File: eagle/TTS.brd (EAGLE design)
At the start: 35.2 x 26.7 mm, 14 parts, among them IC1 LM386N-1

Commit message: updates after build #1
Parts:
- C2, C3: device resistor:C025-025X050 -> rcl:C050-024X044
- R3: value 10k -> 10R
- moved JP1 21.6 mm to (44.5, 33.0), turned to 0 degrees
- moved C6 12.7 mm to (34.3, 44.5)
- moved C2 6.84 mm to (29.2, 41.9), turned to 90 degrees
- moved C3 5.08 mm to (35.6, 39.4), turned to 180 degrees
- moved C1 4.02 mm to (55.9, 33.0), turned to 180 degrees
- moved R2 4.02 mm to (33.0, 35.6), turned to 0 degrees
- moved R1 4.02 mm to (33.0, 33.0), turned to 180 degrees
- moved R4 2.84 mm to (34.3, 50.8), turned to 180 degrees
- moved R3 1.27 mm to (53.3, 36.8), turned to 180 degrees
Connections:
- net N$2: now also R1.2, R2.1; no longer R1.1, R2.2
- net N$3: now also R2.2; no longer R1.2
- net N$7: now also R1.1; no longer R2.1
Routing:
- net GND: track 57.8 -> 0.00 mm
- net VCC: track 22.8 -> 9.40 mm
- net N$9: track 18.3 -> 8.13 mm
- net N$2: track 15.6 -> 7.15 mm
- net N$5: track 12.2 -> 6.14 mm
- net N$3: track 12.5 -> 10.0 mm
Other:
- board text added: "TTS #2"
- board text removed: "TTS #1"

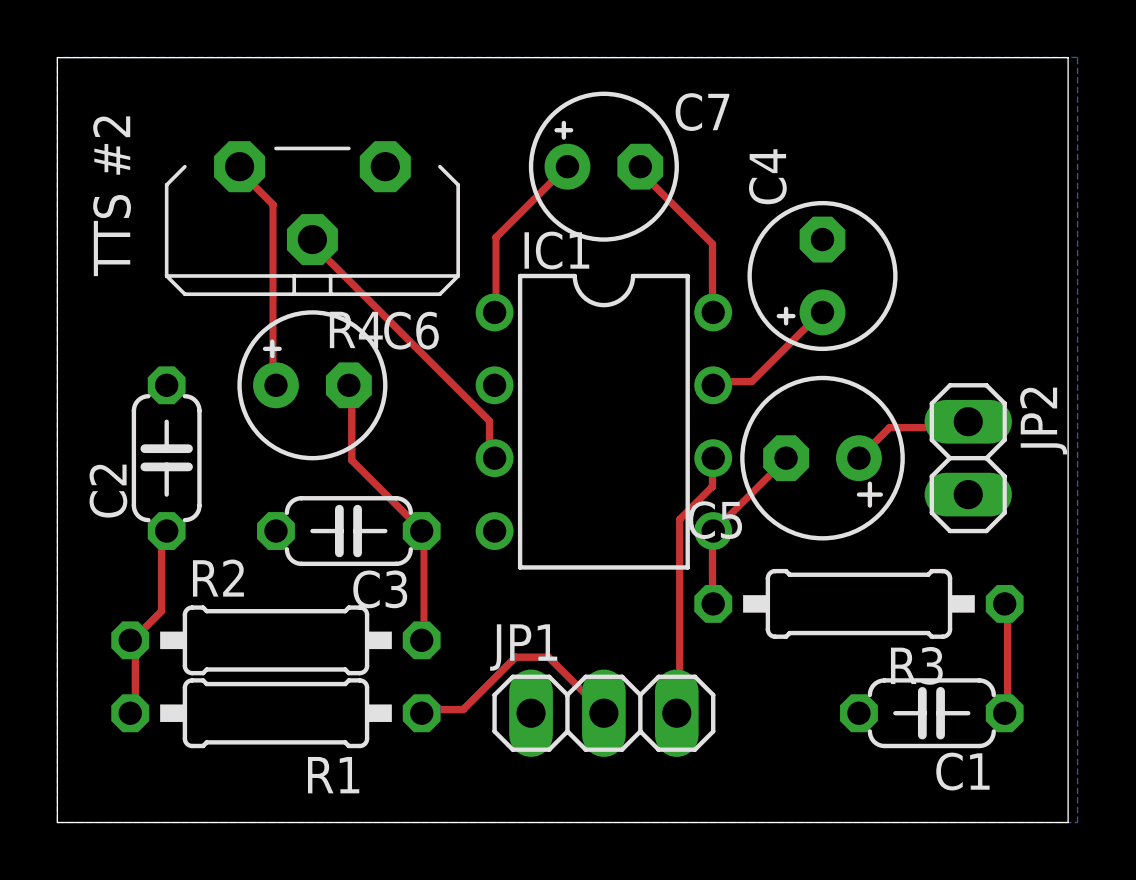
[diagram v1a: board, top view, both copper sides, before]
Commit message: improve board labels
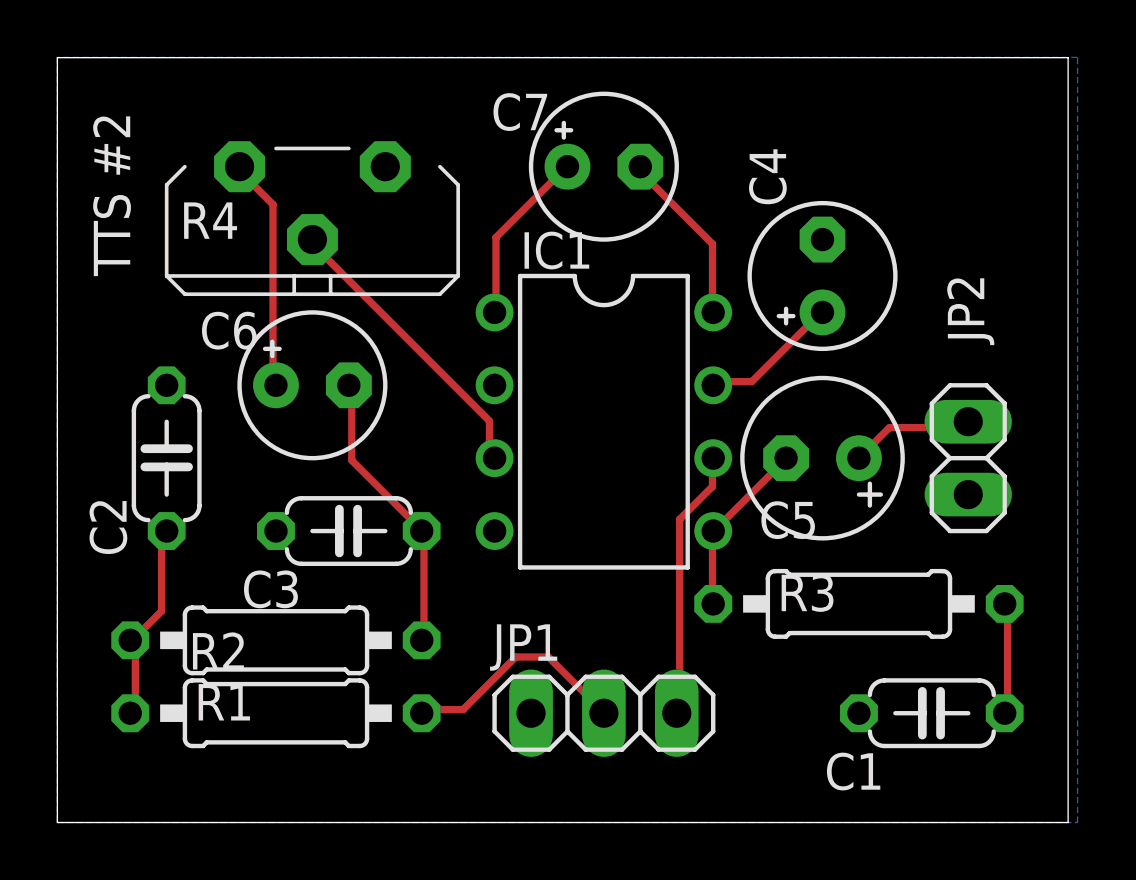
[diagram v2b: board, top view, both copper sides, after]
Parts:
- JP1: value In -> - In +
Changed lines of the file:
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@@
 </autorouter>
 <elements>
-<element name="C1" library="resistor" package="C050-024X044" value="100n" x="55.88" y="33.02" rot="R180"/>
+<element name="C1" library="resistor" package="C050-024X044" value="100n" x="55.88" y="33.02" smashed="yes" rot="R180">
+<attribute name="NAME" x="54.229" y="31.623" size="1.27" layer="25" ratio="10" rot="R180"/>
+<attribute name="VALUE" x="59.309" y="31.877" size="1.27" layer="27" ratio="10" rot="R180"/>
+</element>
 <element name="C4" library="rcl" package="E2,5-5" value="10u" x="52.07" y="48.26" rot="R90"/>
-<element name="C5" library="rcl" package="E2,5-6" value="100u" x="52.07" y="41.91" rot="R180"/>
-<element name="C6" library="rcl" package="E2,5-5" value="10u" x="34.29" y="44.45"/>
-<element name="C7" library="rcl" package="E2,5-5" value="10u" x="44.45" y="52.07"/>
+<element name="C5" library="rcl" package="E2,5-6" value="100u" x="52.07" y="41.91" smashed="yes" rot="R180">
+<attribute name="NAME" x="51.943" y="40.386" size="1.27" layer="25" ratio="10" rot="R180"/>
+<attribute name="VALUE" x="55.753" y="39.497" size="1.27" layer="27" ratio="10" rot="R180"/>
+</element>
+<element name="C6" library="rcl" package="E2,5-5" value="10u" x="34.29" y="44.45" smashed="yes">
+<attribute name="NAME" x="30.353" y="45.72" size="1.27" layer="25" ratio="10"/>
+<attribute name="VALUE" x="36.703" y="45.847" size="1.27" layer="27" ratio="10"/>
+</element>
+<element name="C7" library="rcl" package="E2,5-5" value="10u" x="44.45" y="52.07" smashed="yes">
+<attribute name="NAME" x="40.513" y="53.34" size="1.27" layer="25" ratio="10"/>
+<attribute name="VALUE" x="46.863" y="53.467" size="1.27" layer="27" ratio="10"/>
+</element>
 <element name="IC1" library="linear" package="DIL08" value="LM386N-1" x="44.45" y="43.18" rot="R270"/>
-<element name="JP1" library="pinhead" package="1X03" value="In" x="44.45" y="33.02"/>
-<element name="JP2" library="pinhead" package="1X02" value="Out" x="57.15" y="41.91" rot="R270"/>
-<element name="R2" library="resistor" package="0207/10" value="27k" x="33.02" y="35.56"/>
-<element name="R1" library="resistor" package="0207/10" value="27k" x="33.02" y="33.02" rot="R180"/>
-<element name="R3" library="resistor" package="0207/10" value="10R" x="53.34" y="36.83" rot="R180"/>
-<element name="R4" library="rcl" package="PT-10S" value="10k" x="34.29" y="50.8" rot="R180"/>
-<element name="C2" library="rcl" package="C050-024X044" value="10n" x="29.21" y="41.91" rot="R90"/>
-<element name="C3" library="rcl" package="C050-024X044" value="10n" x="35.56" y="39.37" rot="R180"/>
+<element name="JP1" library="pinhead" package="1X03" value="- In +" x="44.45" y="33.02" smashed="yes">
+<attribute name="NAME" x="40.5638" y="34.8488" size="1.27" layer="25" ratio="10"/>
+<attribute name="VALUE" x="44.45" y="29.845" size="1.27" layer="27" align="bottom-center"/>
+</element>
+<element name="JP2" library="pinhead" package="1X02" value="Out" x="57.15" y="41.91" smashed="yes" rot="R270">
+<attribute name="NAME" x="56.4388" y="48.3362" size="1.27" layer="25" ratio="10" rot="R270"/>
+<attribute name="VALUE" x="59.055" y="43.18" size="1.27" layer="27" rot="R270"/>
+</element>
+<element name="R2" library="resistor" package="0207/10" value="27k" x="33.02" y="35.56" smashed="yes">
+<attribute name="NAME" x="29.972" y="34.544" size="1.27" layer="25" ratio="10"/>
+<attribute name="VALUE" x="33.2994" y="34.925" size="1.27" layer="27" ratio="10"/>
+</element>
+<element name="R1" library="resistor" package="0207/10" value="27k" x="33.02" y="33.02" smashed="yes" rot="R180">
+<attribute name="NAME" x="32.258" y="34.036" size="1.27" layer="25" ratio="10" rot="R180"/>
+<attribute name="VALUE" x="35.2806" y="33.655" size="1.27" layer="27" ratio="10" rot="R180"/>
+</element>
+<element name="R3" library="resistor" package="0207/10" value="10R" x="53.34" y="36.83" smashed="yes" rot="R180">
+<attribute name="NAME" x="52.578" y="37.846" size="1.27" layer="25" ratio="10" rot="R180"/>
+<attribute name="VALUE" x="56.8706" y="37.465" size="1.27" layer="27" ratio="10" rot="R180"/>
+</element>
+<element name="R4" library="rcl" package="PT-10S" value="10k" x="34.29" y="50.8" smashed="yes" rot="R180">
+<attribute name="NAME" x="31.75" y="50.8254" size="1.27" layer="25" ratio="10" rot="R180"/>
+<attribute name="VALUE" x="38.1" y="49.9364" size="1.27" layer="27" ratio="10" rot="R180"/>
+</element>
+<element name="C2" library="rcl" package="C050-024X044" value="10n" x="29.21" y="41.91" smashed="yes" rot="R90">
+<attribute name="NAME" x="27.813" y="38.481" size="1.27" layer="25" ratio="10" rot="R90"/>
+<attribute name="VALUE" x="28.067" y="42.291" size="1.27" layer="27" ratio="10" rot="R90"/>
+</element>
+<element name="C3" library="rcl" package="C050-024X044" value="10n" x="35.56" y="39.37" smashed="yes" rot="R180">
+<attribute name="NAME" x="33.909" y="37.973" size="1.27" layer="25" ratio="10" rot="R180"/>
+<attribute name="VALUE" x="37.719" y="38.227" size="1.27" layer="27" ratio="10" rot="R180"/>
+</element>
 </elements>
 <signals>
